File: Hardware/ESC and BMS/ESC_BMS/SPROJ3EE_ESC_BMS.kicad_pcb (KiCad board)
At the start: 4 copper layers, 100 x 40 mm, 100 parts, among them J301 SW IN, J302 SW OUT, J401 1mm2_connector, J402 1mm2_connector, J403 1mm2_connector, J404 JST_8PH_2mm, J405 JST_3PH_2mm, J406 1mm2_connector, J407 1mm2_connector, J408 1mm2_connector, J409 1mm2_connector, J410 Barrel_Jack_Switch, Q201 SiR696DP, Q202 SiR696DP, Q203 SiR696DP, Q204 SiR696DP, Q205 SiR696DP, Q206 SiR696DP, Q301 SQJQ131EL, Q303 FDV304P, Q304 PMV20XNEA, Q305 SQJQ131EL, Q306 SQJQ131EL, U201 74AUC2G08, U202 74AUC2G08, U203 SN74LVC1G00DBV, U204 SN74LVC1G00DBV, U205 IR2301, U206 IR2301, U207 74AUC2G08, U208 SN74LVC1G00DBV, U209 TL331, U210 IR2301, U301 BQ2057W, U302 BQ2969

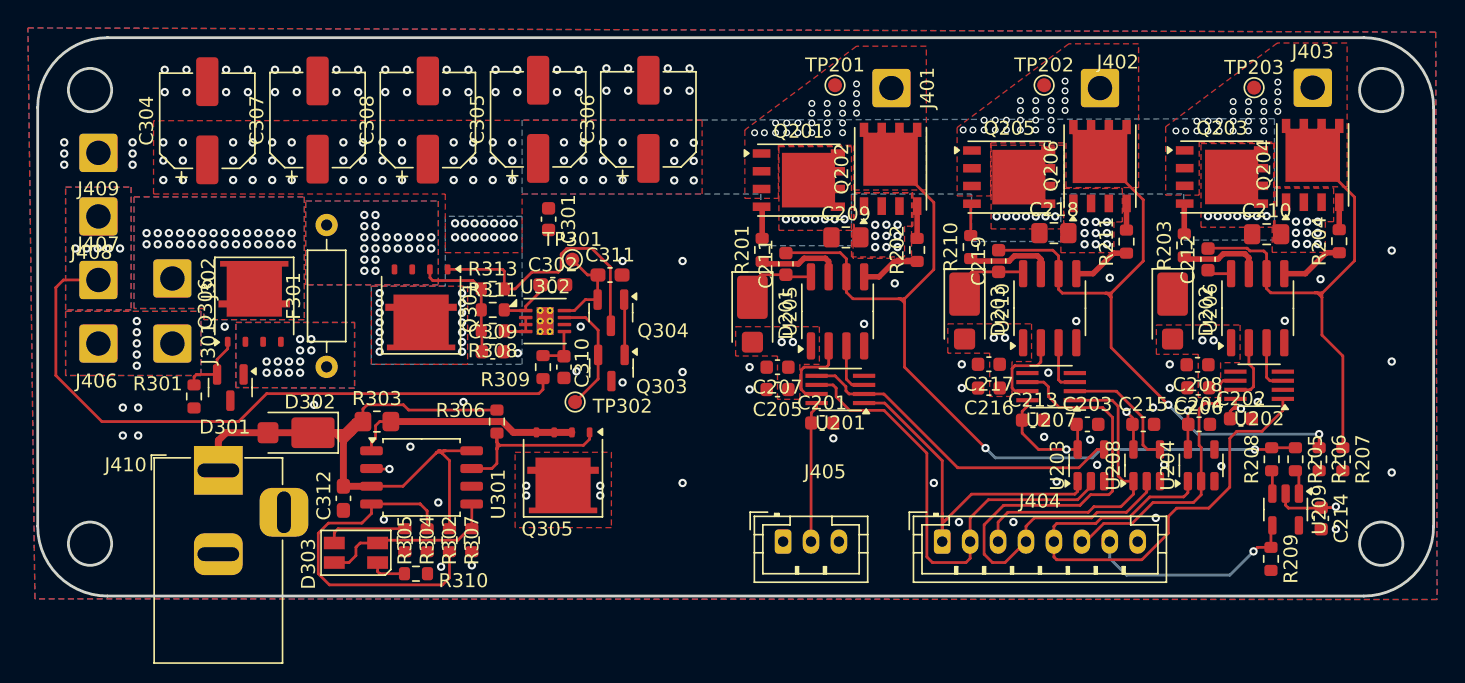
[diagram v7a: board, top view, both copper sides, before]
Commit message: ESC/BMS board done fully
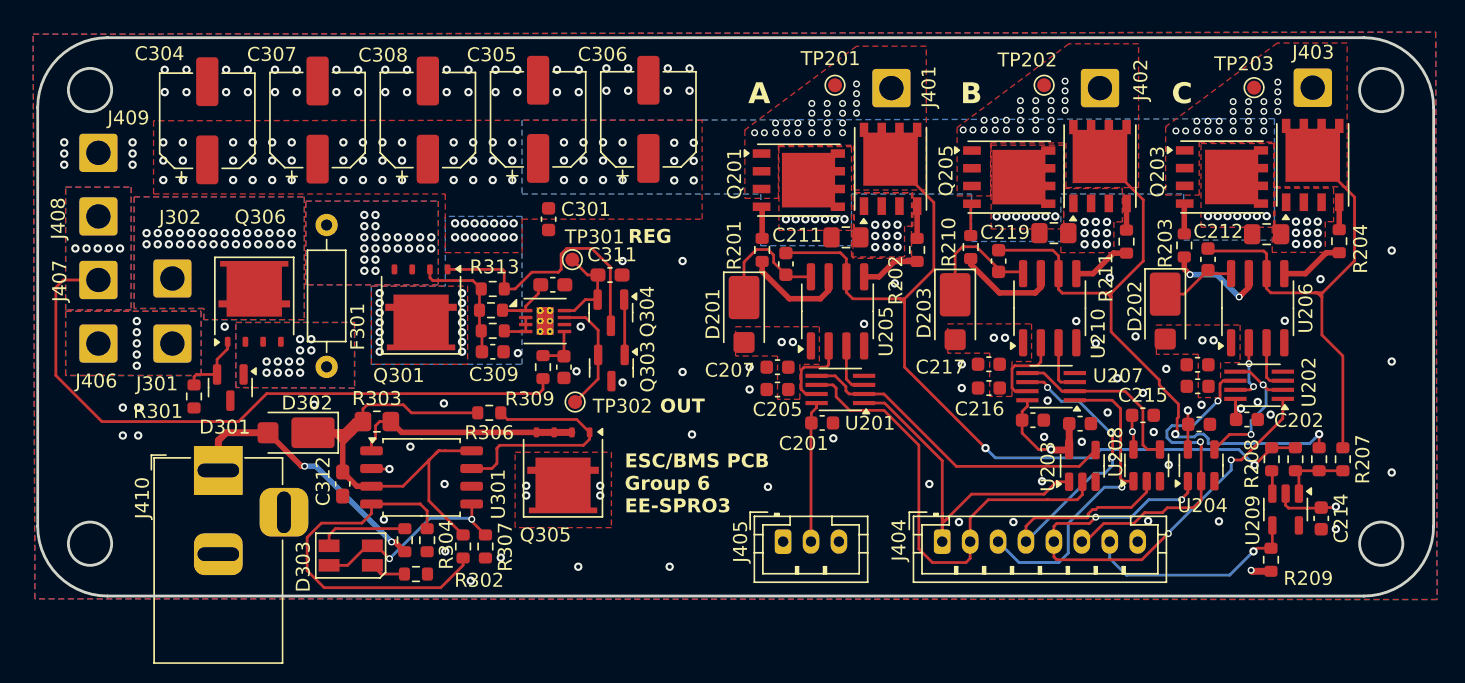
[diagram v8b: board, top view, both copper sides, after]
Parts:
- moved R307 1.07 mm to (127.1, 106.8)
- moved R302 1.07 mm to (125.5, 106.8)
- moved C312 1.03 mm to (116.8, 102.3)
- moved R306 0.83 mm to (127.3, 97.2), turned to 0 degrees
- moved D203 0.68 mm to (160.7, 89.9)
- moved C215 0.65 mm to (174.2, 97.3)
- moved U203 0.61 mm to (169.8, 101.0)
- moved D201 0.60 mm to (145.6, 90.1)
- moved C203 0.53 mm to (169.7, 98.0)
- moved D202 0.53 mm to (175.8, 89.9)
- moved C202 0.43 mm to (181.6, 97.7)
- moved D303 0.43 mm to (117.4, 107.4)
- moved R311 0.13 mm to (127.5, 89.8)
- moved C206 0.11 mm to (178.1, 95.3)
- moved R209 0.06 mm to (183.3, 107.7)
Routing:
- net /1. ESC/CNAND: track 0.00 -> 11.1 mm, vias 0 -> 2
- net /2. BMS/+VCHARGE: track 8.93 -> 19.8 mm, vias 0 -> 2
- net /1. ESC/BLS: track 40.5 -> 30.1 mm, vias 0 -> 3
- net Net-(Q305-G): track 12.6 -> 17.4 mm
- net /1. ESC/BNAND: track 8.97 -> 13.3 mm
- net /1. ESC/CLS: track 20.3 -> 24.1 mm, vias 0 -> 2
- net Net-(D202-K): track 1.76 -> 5.53 mm
- net Net-(U209--): track 1.74 -> 5.14 mm
- net Net-(D203-K): track 5.54 -> 8.92 mm
- net Net-(D201-K): track 5.51 -> 8.83 mm
- net +3.3V: track 99.7 -> 102.1 mm, vias 4 -> 5
- net Net-(D303-A1): track 13.0 -> 15.0 mm, vias 0 -> 2
- net B_PHASE: track 45.6 -> 47.7 mm
- net /1. ESC/CHS: track 38.2 -> 36.3 mm, vias 0 -> 4
- net Net-(D302-K): track 42.7 -> 41.0 mm
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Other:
- board text added: "A"
- board text added: "B"
- board text added: "C"
- board text added: "ESC/BMS PCB Group 6 EE-SPRO3"
- board text added: "OUT"
- board text added: "REG"
